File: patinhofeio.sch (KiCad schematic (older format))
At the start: 0 parts

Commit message: wip
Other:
- note added: "OK"
- note added: "TO-DO!"
- note added: "W.I.P."
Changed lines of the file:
@@
 LIBS:7451
 LIBS:patinhofeio-cache
-EELAYER 27 0
+EELAYER 25 0
 EELAYER END
 $Descr A4 11693 8268
@@
 F1 "prancha-I.sch" 50
 $EndSheet
+Text Notes 2950 2950 0    60   ~ 0
+TO-DO!
+Text Notes 2950 3550 0    60   ~ 0
+TO-DO!
+Text Notes 2950 4150 0    60   ~ 0
+TO-DO!
+Text Notes 1300 4700 0    118  ~ 0
+OK
+Text Notes 5350 2950 0    60   ~ 0
+TO-DO!
+Text Notes 5350 3550 0    60   ~ 0
+TO-DO!
+Text Notes 5350 4150 0    60   ~ 0
+TO-DO!
+Text Notes 5350 4750 0    60   ~ 0
+TO-DO!
+Text Notes 7750 2950 0    60   ~ 0
+TO-DO!
+Text Notes 6050 3500 0    118  ~ 0
+OK
+Text Notes 7750 4150 0    60   ~ 0
+TO-DO!
+Text Notes 7750 4750 0    60   ~ 0
+TO-DO!
+Text Notes 8450 2900 0    118  ~ 0
+W.I.P.
+Text Notes 8450 3500 0    118  ~ 0
+W.I.P.
+Text Notes 10150 4150 0    60   ~ 0
+TO-DO!
+Text Notes 8450 4700 0    118  ~ 0
+OK
 $EndSCHEMATC

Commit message: finalizei a transcrição da prancha XIV! E gerei um PDF dos esquemáticos (incompletos).
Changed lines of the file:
@@
 W.I.P.
 Text Notes 8450 3500 0    118  ~ 0
-W.I.P.
+OK
 Text Notes 10150 4150 0    60   ~ 0
 TO-DO!

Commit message: atualizando o PDF
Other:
- note removed: "W.I.P."
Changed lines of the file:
@@
 TO-DO!
 Text Notes 8450 2900 0    118  ~ 0
-W.I.P.
+OK
 Text Notes 8450 3500 0    118  ~ 0
 OK

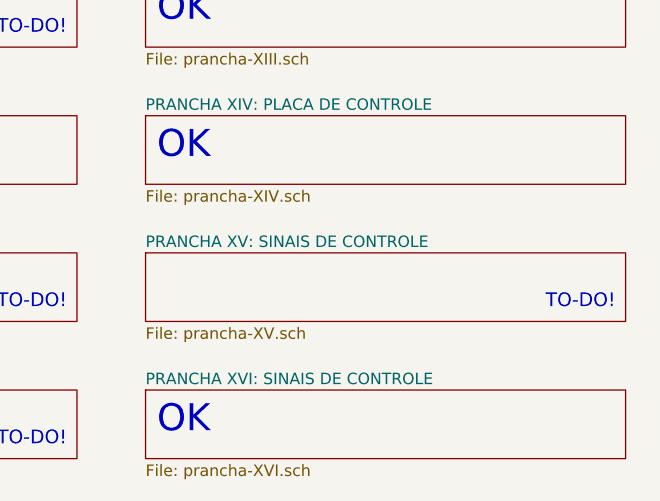
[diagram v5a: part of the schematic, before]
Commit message: mais um pouco de transcrição, agora na prancha 15
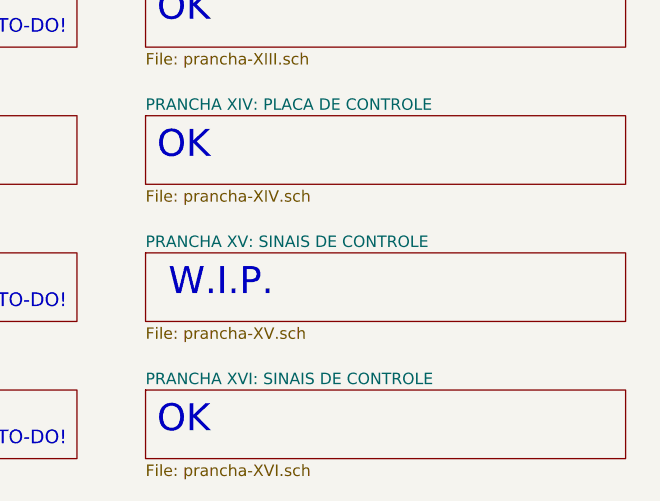
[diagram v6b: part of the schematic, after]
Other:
- note added: "W.I.P."
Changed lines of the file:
@@
 Text Notes 8450 3500 0    118  ~ 0
 OK
-Text Notes 10150 4150 0    60   ~ 0
-TO-DO!
 Text Notes 8450 4700 0    118  ~ 0
 OK
+Text Notes 8500 4100 0    118  ~ 0
+W.I.P.
 $EndSCHEMATC

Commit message: redimensionando todas pranchas para tamanho A2
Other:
- note removed: "W.I.P."
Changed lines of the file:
@@
 OK
 Text Notes 8500 4100 0    118  ~ 0
-W.I.P.
+OK
 $EndSCHEMATC

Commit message: terminei a transcrição da prancha 9!
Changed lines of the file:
@@
 Text Notes 5350 4750 0    60   ~ 0
-TO-DO!
-Text Notes 7750 2950 0    60   ~ 0
 TO-DO!
 Text Notes 6050 3500 0    118  ~ 0
@@
 Text Notes 8500 4100 0    118  ~ 0
 OK
+Text Notes 6050 2900 0    118  ~ 0
+OK
 $EndSCHEMATC
